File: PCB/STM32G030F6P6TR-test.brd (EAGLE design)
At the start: 35.6 x 35.6 mm, 37 parts, among them J1 10118193-0001LF, U1 CP2104-F03-GM, U5 SHT30-DIS-B

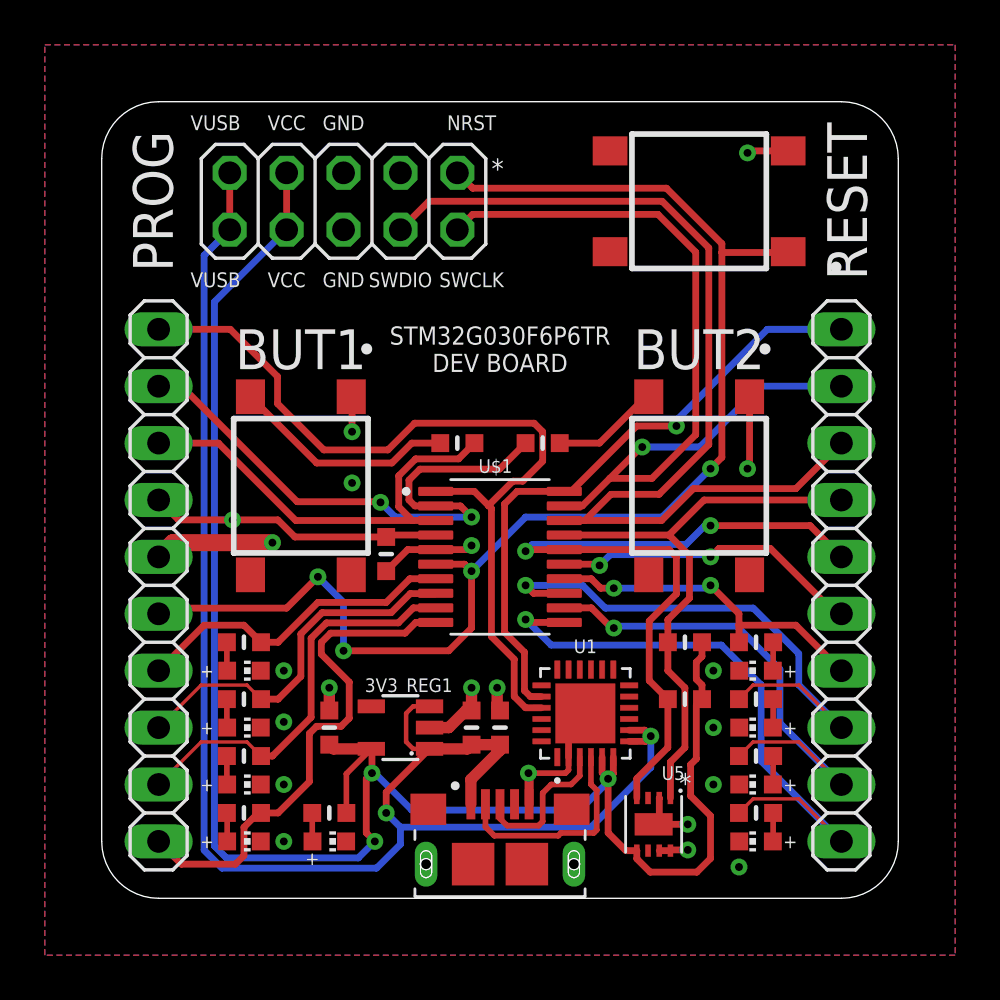
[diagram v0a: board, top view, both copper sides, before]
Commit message: Updated render, revered mounting headers
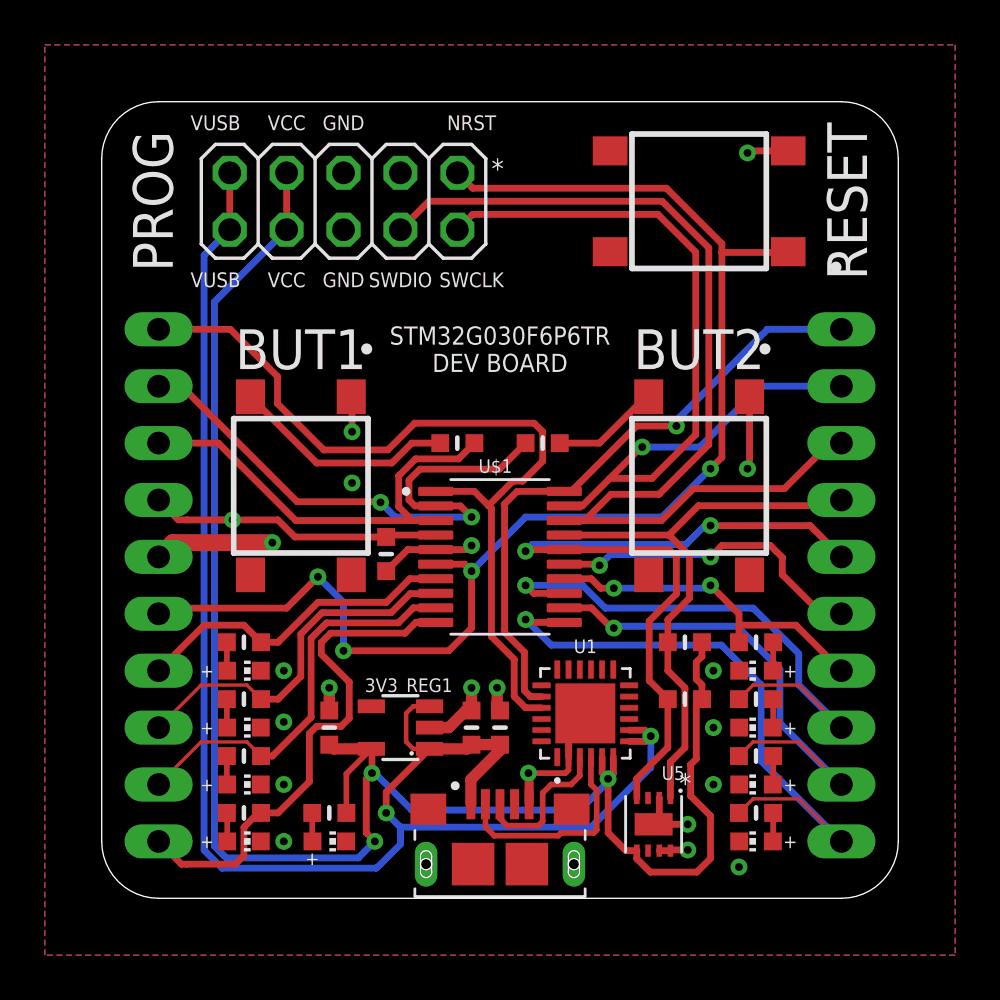
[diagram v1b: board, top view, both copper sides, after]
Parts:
- flipped JP2 to the bottom
- flipped JP3 to the bottom
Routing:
- net PA8: track 14.0 -> 14.6 mm
